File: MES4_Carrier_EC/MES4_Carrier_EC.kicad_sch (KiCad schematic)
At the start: 0 parts

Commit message: Add module finger map page and FE-URT-2 3.3 V note
New page 11 (Pinout): a KiCad table of every MES4-MCU finger with its
STM32 port, function, what this carrier connects to it, the carrier
parts, the MES4-CIF §2c standard use and notes. It follows the MES4-MCU
U1 pin map style (colour-coded Function column, spanned finger-group
rows); the PA0-PA3 rows mark where this board differs from §2c. The
builder gains table() with per-cell fills and row spans, and cell text
resolves {tag} references.

The AuxPower servo note, README and HANDOFF now say to set the FE-URT-2
level switch to 3.3 V: at 5 V its TX exceeds PA3's limit while the
module is unpowered and back-feeds the 3V3 through the RX pull-up.

Co-Authored-By: Claude Opus 5.5 <noreply@anthropic.com>
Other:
- added sheet Pinout (Pinout.kicad_sch)
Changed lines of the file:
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@@
 		(effects (font (size 2.2 2.2) (bold yes)) (justify left top))
 	)
-	(text "E-Crawler carrier for one MES4-MCU module (MES4-CIF rev A-d6). Circuits taken from the MES4-Flasher: PC817 sensor inputs,\nADS1232 load cell, relay channels (driver, INA226) and the XT30 / URB2405S 24 V input.\nGPIO budget: 4 relay drives + ALERT + 3 ADS1232 + 2 sensors + winch (2) + servo USART2 (2) = 14.\nDiffers from the MES4-CIF §2c table: no relay coil feedback, so PA0-PA3 drive the winch and the servo UART.\nRelay drive per CIF §7a (AO3400A, 100 Ω, 100k pull-down); the Flasher uses a 2SC2884 BJT for the same job.\nNo hot-plug: unplug the 24 V XT30 before inserting or removing the module.\nPages: Main (2), CAN (3), Power (4), Relays 1-2 (5), Relays 3-4 (6), Sensors (7), LoadCell (8), AuxPower (9), Winch (10)."
+	(text "E-Crawler carrier for one MES4-MCU module (MES4-CIF rev A-d6). Circuits taken from the MES4-Flasher: PC817 sensor inputs,\nADS1232 load cell, relay channels (driver, INA226) and the XT30 / URB2405S 24 V input.\nGPIO budget: 4 relay drives + ALERT + 3 ADS1232 + 2 sensors + winch (2) + servo USART2 (2) = 14.\nDiffers from the MES4-CIF §2c table: no relay coil feedback, so PA0-PA3 drive the winch and the servo UART.\nRelay drive per CIF §7a (AO3400A, 100 Ω, 100k pull-down); the Flasher uses a 2SC2884 BJT for the same job.\nNo hot-plug: unplug the 24 V XT30 before inserting or removing the module.\nPages: Main (2), CAN (3), Power (4), Relays 1-2 (5), Relays 3-4 (6), Sensors (7), LoadCell (8), AuxPower (9), Winch (10), Pinout (11)."
 		(exclude_from_sim no)
 		(at 20.32 221 0)
@@
 		(instances
 			(project "MES4_Carrier_EC"
-				(path "/20e873b0-a362-5816-a506-9e1cffc294d3"
+				(path "/da774ca2-fff6-5e5d-8e21-ede9d04ec2cb"
 					(page "2")
 				)
@@
 		(instances
 			(project "MES4_Carrier_EC"
-				(path "/20e873b0-a362-5816-a506-9e1cffc294d3"
+				(path "/da774ca2-fff6-5e5d-8e21-ede9d04ec2cb"
 					(page "3")
 				)
@@
 		(instances
 			(project "MES4_Carrier_EC"
-				(path "/20e873b0-a362-5816-a506-9e1cffc294d3"
+				(path "/da774ca2-fff6-5e5d-8e21-ede9d04ec2cb"
 					(page "4")
 				)
@@
 		(instances
 			(project "MES4_Carrier_EC"
-				(path "/20e873b0-a362-5816-a506-9e1cffc294d3"
+				(path "/da774ca2-fff6-5e5d-8e21-ede9d04ec2cb"
 					(page "5")
 				)
@@
 		(instances
 			(project "MES4_Carrier_EC"
-				(path "/20e873b0-a362-5816-a506-9e1cffc294d3"
+				(path "/da774ca2-fff6-5e5d-8e21-ede9d04ec2cb"
 					(page "6")
 				)
@@
 		(instances
 			(project "MES4_Carrier_EC"
-				(path "/20e873b0-a362-5816-a506-9e1cffc294d3"
+				(path "/da774ca2-fff6-5e5d-8e21-ede9d04ec2cb"
 					(page "7")
 				)
@@
 		(instances
 			(project "MES4_Carrier_EC"
-				(path "/20e873b0-a362-5816-a506-9e1cffc294d3"
+				(path "/da774ca2-fff6-5e5d-8e21-ede9d04ec2cb"
 					(page "8")
 				)
@@
 		(instances
 			(project "MES4_Carrier_EC"
-				(path "/20e873b0-a362-5816-a506-9e1cffc294d3"
+				(path "/da774ca2-fff6-5e5d-8e21-ede9d04ec2cb"
 					(page "9")
 				)
@@
 		(instances
 			(project "MES4_Carrier_EC"
-				(path "/20e873b0-a362-5816-a506-9e1cffc294d3"
+				(path "/da774ca2-fff6-5e5d-8e21-ede9d04ec2cb"
 					(page "10")
 				)
 			)
+		)
+	)
+	(sheet
+		(at 373.38 236.22)
+		(size 26.67 7.62)
+		(exclude_from_sim no)
+		(in_bom yes)
+		(on_board yes)
+		(dnp no)
+		(stroke (width 0.35) (type solid) (color 200 110 0 1))
+		(fill (color 255 240 220 1))
+		(property "Sheetname" "Pinout"
+			(at 373.38 235.51 0)
+			(effects (font (size 2 2) (thickness 0.4) (bold yes)) (justify left bottom))
+		)
+		(property "Sheetfile" "Pinout.kicad_sch"
+			(at 373.38 244.6 0)
+			(effects (font (size 1.27 1.27)) (justify left top))
+		)
+		(instances
+			(project "MES4_Carrier_EC"
+				(path "/da774ca2-fff6-5e5d-8e21-ede9d04ec2cb"
+					(page "11")
+				)
+			)

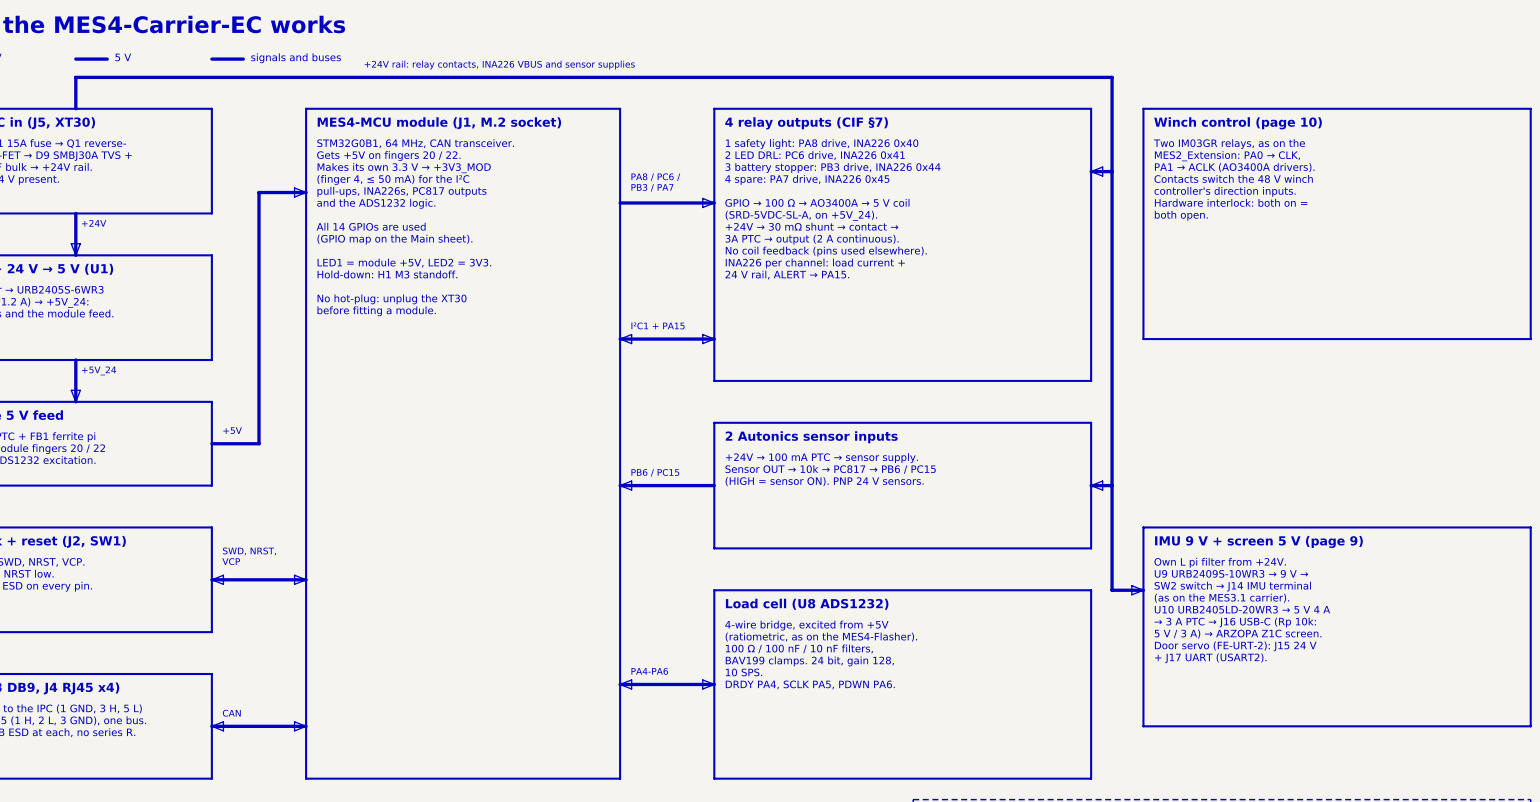
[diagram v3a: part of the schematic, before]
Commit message: Isolate the 48 V winch side, add servo TX pull-up, tidy block diagram
Winch: J18 and the WINCH_* / ILK_* nets already touch only relay
contacts; they now form net class Winch_48V (0.6 mm clearance), and the
Winch sheet, README and HANDOFF state the isolation rules (>= 2 mm to
other copper, no GND pour under J18, no ESD to GND on J18).

Servo: R37 10k pull-up holds PA2 (TX) idle HIGH while the MCU is in
reset. AuxPower/Winch refs R37-R45 shift by one; README follows, and the
LED8 resistor ref is corrected to R35.

Block diagram: door servo block, winch and servo links from the module,
24 V routed so it never crosses a signal line, channel lines on an even
5.08 mm pitch.

Co-Authored-By: Claude Opus 5.5 <noreply@anthropic.com>
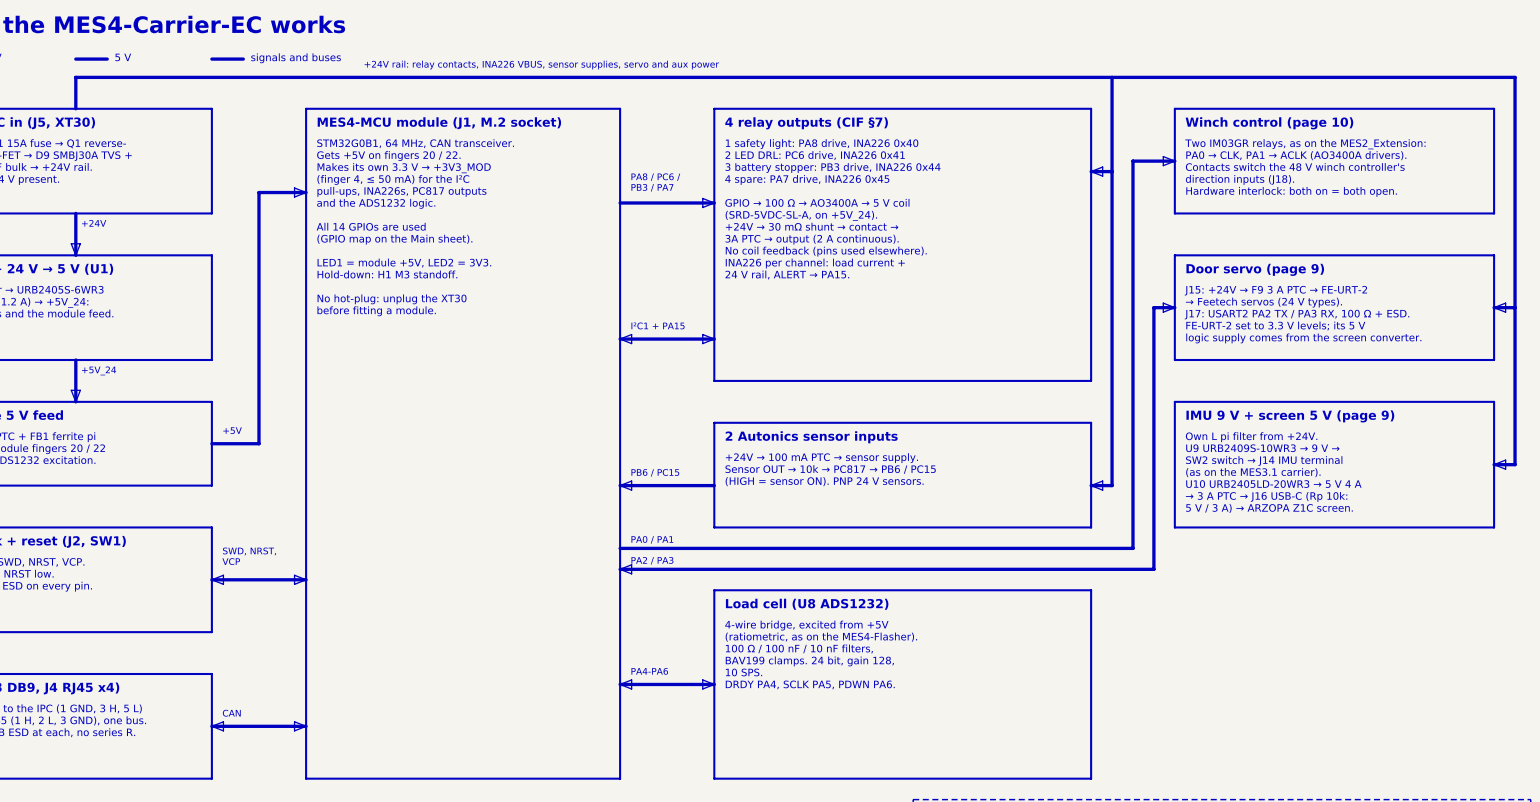
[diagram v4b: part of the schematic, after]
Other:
- note added: "+24V rail: relay contacts, INA226 VBUS, sensor supplies, servo and aux power"
- note added: "Door servo (page 9)"
- note added: "J15: +24V → F9 3 A PTC → FE-URT-2 → Feetech servos (24 V types). J17: USART2 PA2 TX / PA3 RX, 100 Ω + ESD. FE-URT-2 set to 3.3 V levels; its 5 V logic supply comes from the screen converter."
- note added: "Own L pi filter from +24V. U9 URB2409S-10WR3 → 9 V → SW2 switch → J14 IMU terminal (as on the MES3.1 carrier). U10 URB2405LD-20WR3 → 5 V 4 A → 3 A PTC → J16 USB-C (Rp 10k: 5 V / 3 A) → ARZOPA Z1C screen."
- note added: "PA0 / PA1"
- note added: "PA2 / PA3"
- note added: "Two IM03GR relays, as on the MES2_Extension: PA0 → CLK, PA1 → ACLK (AO3400A drivers). Contacts switch the 48 V winch controller's direction inputs (J18). Hardware interlock: both on = both open."
- note removed: "+24V rail: relay contacts, INA226 VBUS and sensor supplies"
- note removed: "Own L pi filter from +24V. U9 URB2409S-10WR3 → 9 V → SW2 switch → J14 IMU terminal (as on the MES3.1 carrier). U10 URB2405LD-20WR3 → 5 V 4 A → 3 A PTC → J16 USB-C (Rp 10k: 5 V / 3 A) → ARZOPA Z1C screen. Door servo (FE-URT-2): J15 24 V + J17 UART (USART2)."
- note removed: "Two IM03GR relays, as on the MES2_Extension: PA0 → CLK, PA1 → ACLK (AO3400A drivers). Contacts switch the 48 V winch controller's direction inputs. Hardware interlock: both on = both open."
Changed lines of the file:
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@@
 	(rectangle
 		(start 205.74 116.84)
-		(end 297.18 147.32)
+		(end 297.18 142.24)
 		(stroke (width 0.5) (type solid) (color 200 30 30 1))
 		(fill (type color) (color 222 242 222 1))
@@
 	)
 	(polyline
-		(pts (xy 50.8 40.64) (xy 50.8 33.02) (xy 302.26 33.02) (xy 302.26 132.08))
+		(pts (xy 50.8 40.64) (xy 50.8 33.02) (xy 400.05 33.02) (xy 400.05 127))
+		(stroke (width 0.8) (type solid) (color 200 30 30 1))
+		(fill (type none))
+	)
+	(polyline
+		(pts (xy 302.26 33.02) (xy 302.26 132.08))
 		(stroke (width 0.8) (type solid) (color 200 30 30 1))
 		(fill (type none))
@@
 		(fill (type color) (color 200 30 30 1))
 	)
-	(text "+24V rail: relay contacts, INA226 VBUS and sensor supplies"
+	(text "+24V rail: relay contacts, INA226 VBUS, sensor supplies, servo and aux power"
 		(exclude_from_sim no)
 		(at 120.65 29.21 0)
@@
 	)
 	(rectangle
-		(start 309.88 142.24)
-		(end 403.86 190.5)
+		(start 317.5 40.64)
+		(end 394.97 66.04)
+		(stroke (width 0.5) (type solid) (color 110 110 110 1))
+		(fill (type color) (color 238 238 238 1))
+	)
+	(text "Winch control (page 10)"
+		(exclude_from_sim no)
+		(at 320.04 42.93 0)
+		(effects (font (size 2.2 2.2) (bold yes)) (justify left top))
+	)
+	(text "Two IM03GR relays, as on the MES2_Extension:\nPA0 → CLK, PA1 → ACLK (AO3400A drivers).\nContacts switch the 48 V winch controller's\ndirection inputs (J18).\nHardware interlock: both on = both open."
+		(exclude_from_sim no)
+		(at 320.04 48.26 0)
+		(effects (font (size 1.8 1.8)) (justify left top))
+	)
+	(rectangle
+		(start 317.5 76.2)
+		(end 394.97 101.6)
+		(stroke (width 0.5) (type solid) (color 200 30 30 1))
+		(fill (type color) (color 222 242 222 1))
+	)
+	(text "Door servo (page 9)"
+		(exclude_from_sim no)
+		(at 320.04 78.49 0)
+		(effects (font (size 2.2 2.2) (bold yes)) (justify left top))
+	)
+	(text "J15: +24V → F9 3 A PTC → FE-URT-2\n→ Feetech servos (24 V types).\nJ17: USART2 PA2 TX / PA3 RX, 100 Ω + ESD.\nFE-URT-2 set to 3.3 V levels; its 5 V\nlogic supply comes from the screen converter."
+		(exclude_from_sim no)
+		(at 320.04 83.82 0)
+		(effects (font (size 1.8 1.8)) (justify left top))
+	)
+	(polyline
+		(pts (xy 400.05 88.9) (xy 394.97 88.9))
+		(stroke (width 0.8) (type solid) (color 200 30 30 1))
+		(fill (type none))
+	)
+	(polyline
+		(pts (xy 394.97 88.9) (xy 397.77 87.8) (xy 397.77 90) (xy 394.97 88.9))
+		(stroke (width 0.1) (type solid) (color 200 30 30 1))
+		(fill (type color) (color 200 30 30 1))
+	)
+	(rectangle
+		(start 317.5 111.76)
+		(end 394.97 142.24)
 		(stroke (width 0.5) (type solid) (color 225 115 0 1))
 		(fill (type color) (color 255 238 220 1))
@@
 	(text "IMU 9 V + screen 5 V (page 9)"
 		(exclude_from_sim no)
-		(at 312.42 144.53 0)
+		(at 320.04 114.05 0)
 		(effects (font (size 2.2 2.2) (bold yes)) (justify left top))
 	)
-	(text "Own L pi filter from +24V.\nU9 URB2409S-10WR3 → 9 V →\nSW2 switch → J14 IMU terminal\n(as on the MES3.1 carrier).\nU10 URB2405LD-20WR3 → 5 V 4 A\n→ 3 A PTC → J16 USB-C (Rp 10k:\n5 V / 3 A) → ARZOPA Z1C screen.\nDoor servo (FE-URT-2): J15 24 V\n+ J17 UART (USART2)."
-		(exclude_from_sim no)
-		(at 312.42 149.86 0)
+	(text "Own L pi filter from +24V.\nU9 URB2409S-10WR3 → 9 V →\nSW2 switch → J14 IMU terminal\n(as on the MES3.1 carrier).\nU10 URB2405LD-20WR3 → 5 V 4 A\n→ 3 A PTC → J16 USB-C (Rp 10k:\n5 V / 3 A) → ARZOPA Z1C screen."
+		(exclude_from_sim no)
+		(at 320.04 119.38 0)
 		(effects (font (size 1.8 1.8)) (justify left top))
 	)
 	(polyline
-		(pts (xy 302.26 132.08) (xy 302.26 157.48))
-		(stroke (width 0.8) (type solid) (color 200 30 30 1))
-		(fill (type none))
-	)
-	(rectangle
-		(start 309.88 40.64)
-		(end 403.86 96.52)
-		(stroke (width 0.5) (type solid) (color 110 110 110 1))
-		(fill (type color) (color 238 238 238 1))
-	)
-	(text "Winch control (page 10)"
-		(exclude_from_sim no)
-		(at 312.42 42.93 0)
-		(effects (font (size 2.2 2.2) (bold yes)) (justify left top))
-	)
-	(text "Two IM03GR relays, as on the\nMES2_Extension: PA0 → CLK,\nPA1 → ACLK (AO3400A drivers).\nContacts switch the 48 V winch\ncontroller's direction inputs.\nHardware interlock: both on =\nboth open."
-		(exclude_from_sim no)
-		(at 312.42 48.26 0)
-		(effects (font (size 1.8 1.8)) (justify left top))
-	)
-	(polyline
-		(pts (xy 302.26 157.48) (xy 309.88 157.48))
-		(stroke (width 0.8) (type solid) (color 200 30 30 1))
-		(fill (type none))
-	)
-	(polyline
-		(pts (xy 309.88 157.48) (xy 307.08 158.58) (xy 307.08 156.38) (xy 309.88 157.48))
+		(pts (xy 400.05 127) (xy 394.97 127))
+		(stroke (width 0.8) (type solid) (color 200 30 30 1))
+		(fill (type none))
+	)
+	(polyline
+		(pts (xy 394.97 127) (xy 397.77 125.9) (xy 397.77 128.1) (xy 394.97 127))
 		(stroke (width 0.1) (type solid) (color 200 30 30 1))
 		(fill (type color) (color 200 30 30 1))
+	)
+	(polyline
+		(pts (xy 182.88 147.32) (xy 307.34 147.32) (xy 307.34 53.34) (xy 317.5 53.34))
+		(stroke (width 0.8) (type solid) (color 30 80 200 1))
+		(fill (type none))
+	)
+	(polyline
+		(pts (xy 317.5 53.34) (xy 314.7 54.44) (xy 314.7 52.24) (xy 317.5 53.34))
+		(stroke (width 0.1) (type solid) (color 30 80 200 1))
+		(fill (type color) (color 30 80 200 1))
+	)
+	(text "PA0 / PA1"
+		(exclude_from_sim no)
+		(at 185.42 144.53 0)
+		(effects (font (size 1.6 1.6) (color 30 80 200 1)) (justify left top))
+	)
+	(polyline
+		(pts (xy 182.88 152.4) (xy 312.42 152.4) (xy 312.42 88.9) (xy 317.5 88.9))
+		(stroke (width 0.8) (type solid) (color 30 80 200 1))
+		(fill (type none))
+	)
+	(polyline
+		(pts (xy 317.5 88.9) (xy 314.7 90) (xy 314.7 87.8) (xy 317.5 88.9))
+		(stroke (width 0.1) (type solid) (color 30 80 200 1))
+		(fill (type color) (color 30 80 200 1))
+	)
+	(polyline
+		(pts (xy 182.88 152.4) (xy 185.68 151.3) (xy 185.68 153.5) (xy 182.88 152.4))
+		(stroke (width 0.1) (type solid) (color 30 80 200 1))
+		(fill (type color) (color 30 80 200 1))
+	)
+	(text "PA2 / PA3"
+		(exclude_from_sim no)
+		(at 185.42 149.61 0)
+		(effects (font (size 1.6 1.6) (color 30 80 200 1)) (justify left top))
 	)
 	(polyline
@@
 		(instances
 			(project "MES4_Carrier_EC"
-				(path "/da774ca2-fff6-5e5d-8e21-ede9d04ec2cb"
+				(path "/0370b922-a365-5c71-ab6f-f5cfbc7b5e5a"
 					(page "2")
 				)
@@
 		(instances
 			(project "MES4_Carrier_EC"
-				(path "/da774ca2-fff6-5e5d-8e21-ede9d04ec2cb"
+				(path "/0370b922-a365-5c71-ab6f-f5cfbc7b5e5a"
 					(page "3")
 				)
@@
 		(instances
 			(project "MES4_Carrier_EC"
-				(path "/da774ca2-fff6-5e5d-8e21-ede9d04ec2cb"
+				(path "/0370b922-a365-5c71-ab6f-f5cfbc7b5e5a"
 					(page "4")
 				)
@@
 		(instances
 			(project "MES4_Carrier_EC"
-				(path "/da774ca2-fff6-5e5d-8e21-ede9d04ec2cb"
+				(path "/0370b922-a365-5c71-ab6f-f5cfbc7b5e5a"
 					(page "5")
 				)
@@
 		(instances
 			(project "MES4_Carrier_EC"
-				(path "/da774ca2-fff6-5e5d-8e21-ede9d04ec2cb"
+				(path "/0370b922-a365-5c71-ab6f-f5cfbc7b5e5a"
 					(page "6")
 				)
@@
 		(instances
 			(project "MES4_Carrier_EC"
-				(path "/da774ca2-fff6-5e5d-8e21-ede9d04ec2cb"
+				(path "/0370b922-a365-5c71-ab6f-f5cfbc7b5e5a"
 					(page "7")
 				)
@@
 		(instances
 			(project "MES4_Carrier_EC"
-				(path "/da774ca2-fff6-5e5d-8e21-ede9d04ec2cb"
+				(path "/0370b922-a365-5c71-ab6f-f5cfbc7b5e5a"
 					(page "8")
 				)
@@
 		(instances
 			(project "MES4_Carrier_EC"
-				(path "/da774ca2-fff6-5e5d-8e21-ede9d04ec2cb"
+				(path "/0370b922-a365-5c71-ab6f-f5cfbc7b5e5a"
 					(page "9")
 				)
@@
 		(instances
 			(project "MES4_Carrier_EC"
-				(path "/da774ca2-fff6-5e5d-8e21-ede9d04ec2cb"
+				(path "/0370b922-a365-5c71-ab6f-f5cfbc7b5e5a"
 					(page "10")
 				)
@@
 		(instances
 			(project "MES4_Carrier_EC"
-				(path "/da774ca2-fff6-5e5d-8e21-ede9d04ec2cb"
+				(path "/0370b922-a365-5c71-ab6f-f5cfbc7b5e5a"
 					(page "11")
 				)
